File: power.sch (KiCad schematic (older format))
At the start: 26 parts, among them U24 TLV62569P, U26 TLV62569P, U27 TLV62569P

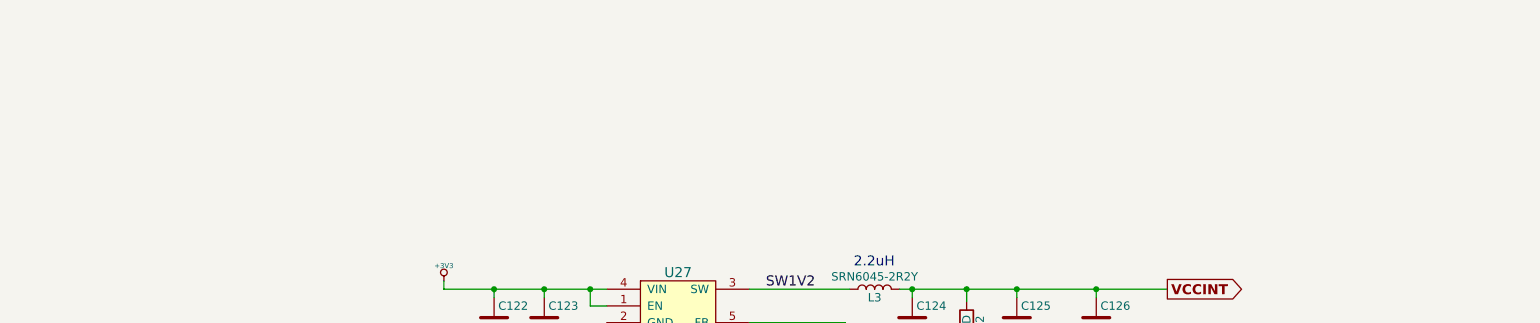
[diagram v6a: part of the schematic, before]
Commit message: VCCA and VCCD_PLL
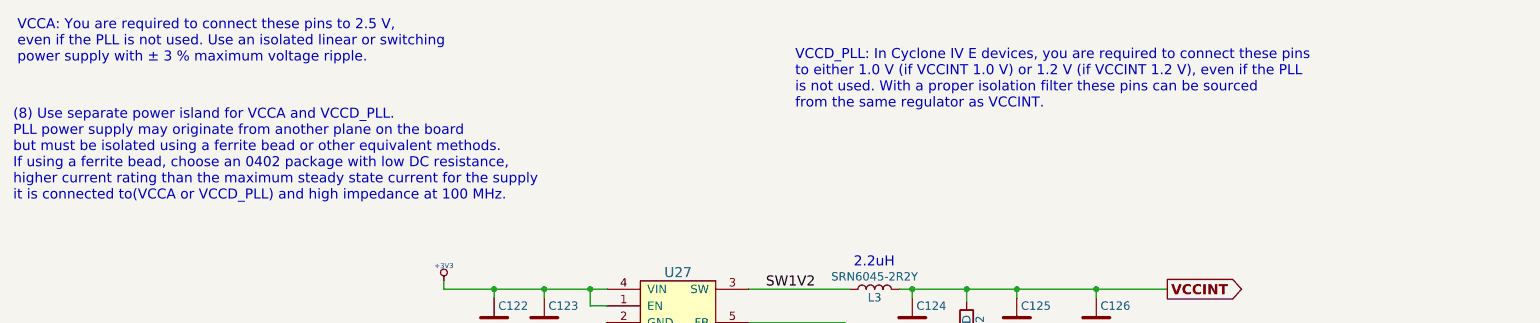
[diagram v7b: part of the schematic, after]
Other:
- note added: "(8) Use separate power island for VCCA and VCCD_PLL. \nPLL power supply may originate from another plane on the board \nbut must be isolated using a ferrite bead or other equivalent methods. \nIf using a ferrite bead, choose an 0402 package with low DC resistance, \nhigher current rating than the maximum steady state current for the supply \nit is connected to(VCCA or VCCD_PLL) and high impedance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"
- note added: "VCCA: You are required to connect these pins to 2.5 V, \neven if the PLL is not used. Use an isolated linear or switching \npower supply with ± 3 % maximum voltage ripple."
- note added: "VCCD_PLL: In Cyclone IV E devices, you are required to connect these pins \nto either 1.0 V (if VCCINT 1.0 V) or 1.2 V (if VCCINT 1.2 V), even if the PLL \nis not used. With a proper isolation filter these pins can be sourced \nfrom the same regulator as VCCINT."
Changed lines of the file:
@@
 $EndComp
 $Comp
-L GND #PWR0182
+L GND #PWR0186
 U 1 1 588CA667
 P 4500 3850
-F 0 "#PWR0182" H 4500 3600 50  0001 C CNN
+F 0 "#PWR0186" H 4500 3600 50  0001 C CNN
 F 1 "GND" H 4500 3700 50  0001 C CNN
 F 2 "" H 4500 3850 50  0000 C CNN
@@
 Connection ~ 4125 3650
 $Comp
-L GND #PWR0183
+L GND #PWR0187
 U 1 1 588CA72B
 P 4125 4000
-F 0 "#PWR0183" H 4125 3750 50  0001 C CNN
+F 0 "#PWR0187" H 4125 3750 50  0001 C CNN
 F 1 "GND" H 4125 3850 50  0001 C CNN
 F 2 "" H 4125 4000 50  0000 C CNN
@@
 	6650 4025 6650 4175
 $Comp
-L GND #PWR0184
+L GND #PWR0188
 U 1 1 588CB06D
 P 6650 4475
-F 0 "#PWR0184" H 6650 4225 50  0001 C CNN
+F 0 "#PWR0188" H 6650 4225 50  0001 C CNN
 F 1 "GND" H 6650 4325 50  0001 C CNN
 F 2 "" H 6650 4475 50  0000 C CNN
@@
 $EndComp
 $Comp
-L GND #PWR0185
+L GND #PWR0189
 U 1 1 588CB1AB
 P 6325 4000
-F 0 "#PWR0185" H 6325 3750 50  0001 C CNN
+F 0 "#PWR0189" H 6325 3750 50  0001 C CNN
 F 1 "GND" H 6325 3850 50  0001 C CNN
 F 2 "" H 6325 4000 50  0000 C CNN
@@
 +1V8
 $Comp
-L +5VDC #PWR0186
+L +5VDC #PWR0190
 U 1 1 588CF502
 P 3525 3600
-F 0 "#PWR0186" H 3625 3650 20  0001 C CNN
+F 0 "#PWR0190" H 3625 3650 20  0001 C CNN
 F 1 "+5VDC" H 3525 3690 30  0000 C CNN
 F 2 "" H 3525 3600 60  0000 C CNN
@@
 Connection ~ 3825 3650
 $Comp
-L GND #PWR0187
+L GND #PWR0191
 U 1 1 588D28B5
 P 3825 4000
-F 0 "#PWR0187" H 3825 3750 50  0001 C CNN
+F 0 "#PWR0191" H 3825 3750 50  0001 C CNN
 F 1 "GND" H 3825 3850 50  0001 C CNN
 F 2 "" H 3825 4000 50  0000 C CNN
@@
 $EndComp
 $Comp
-L GND #PWR0188
+L GND #PWR0192
 U 1 1 58A65167
 P 4500 5175
-F 0 "#PWR0188" H 4500 4925 50  0001 C CNN
+F 0 "#PWR0192" H 4500 4925 50  0001 C CNN
 F 1 "GND" H 4500 5025 50  0001 C CNN
 F 2 "" H 4500 5175 50  0000 C CNN
@@
 Connection ~ 4125 4975
 $Comp
-L GND #PWR0189
+L GND #PWR0193
 U 1 1 58A6517D
 P 4125 5325
-F 0 "#PWR0189" H 4125 5075 50  0001 C CNN
+F 0 "#PWR0193" H 4125 5075 50  0001 C CNN
 F 1 "GND" H 4125 5175 50  0001 C CNN
 F 2 "" H 4125 5325 50  0000 C CNN
@@
 	6650 5350 6650 5500
 $Comp
-L GND #PWR0190
+L GND #PWR0194
 U 1 1 58A6519F
 P 6650 5800
-F 0 "#PWR0190" H 6650 5550 50  0001 C CNN
+F 0 "#PWR0194" H 6650 5550 50  0001 C CNN
 F 1 "GND" H 6650 5650 50  0001 C CNN
 F 2 "" H 6650 5800 50  0000 C CNN
@@
 $EndComp
 $Comp
-L GND #PWR0191
+L GND #PWR0195
 U 1 1 58A651B1
 P 6325 5325
-F 0 "#PWR0191" H 6325 5075 50  0001 C CNN
+F 0 "#PWR0195" H 6325 5075 50  0001 C CNN
 F 1 "GND" H 6325 5175 50  0001 C CNN
 F 2 "" H 6325 5325 50  0000 C CNN
@@
 Connection ~ 3825 4975
 $Comp
-L GND #PWR0192
+L GND #PWR0196
 U 1 1 58A651D3
 P 3825 5325
-F 0 "#PWR0192" H 3825 5075 50  0001 C CNN
+F 0 "#PWR0196" H 3825 5075 50  0001 C CNN
 F 1 "GND" H 3825 5175 50  0001 C CNN
 F 2 "" H 3825 5325 50  0000 C CNN
@@
 $EndComp
 $Comp
-L GND #PWR0193
+L GND #PWR0197
 U 1 1 58A65EC4
 P 7425 5325
-F 0 "#PWR0193" H 7425 5075 50  0001 C CNN
+F 0 "#PWR0197" H 7425 5075 50  0001 C CNN
 F 1 "GND" H 7425 5175 50  0001 C CNN
 F 2 "" H 7425 5325 50  0000 C CNN
@@
 Connection ~ 7425 4975
 $Comp
-L +5VDC #PWR0194
+L +5VDC #PWR0198
 U 1 1 58A651C3
 P 3525 4925
-F 0 "#PWR0194" H 3625 4975 20  0001 C CNN
+F 0 "#PWR0198" H 3625 4975 20  0001 C CNN
 F 1 "+5VDC" H 3525 5015 30  0000 C CNN
 F 2 "" H 3525 4925 60  0000 C CNN
@@
 $EndComp
 $Comp
-L GND #PWR0195
+L GND #PWR0199
 U 1 1 58A865FA
 P 4500 2550
-F 0 "#PWR0195" H 4500 2300 50  0001 C CNN
+F 0 "#PWR0199" H 4500 2300 50  0001 C CNN
 F 1 "GND" H 4500 2400 50  0001 C CNN
 F 2 "" H 4500 2550 50  0000 C CNN
@@
 Connection ~ 4125 2350
 $Comp
-L GND #PWR0196
+L GND #PWR0200
 U 1 1 58A8660D
 P 4125 2700
-F 0 "#PWR0196" H 4125 2450 50  0001 C CNN
+F 0 "#PWR0200" H 4125 2450 50  0001 C CNN
 F 1 "GND" H 4125 2550 50  0001 C CNN
 F 2 "" H 4125 2700 50  0000 C CNN
@@
 	6650 2725 6650 2875
 $Comp
-L GND #PWR0197
+L GND #PWR0201
 U 1 1 58A8662B
 P 6650 3175
-F 0 "#PWR0197" H 6650 2925 50  0001 C CNN
+F 0 "#PWR0201" H 6650 2925 50  0001 C CNN
 F 1 "GND" H 6650 3025 50  0001 C CNN
 F 2 "" H 6650 3175 50  0000 C CNN
@@
 $EndComp
 $Comp
-L GND #PWR0198
+L GND #PWR0202
 U 1 1 58A8663C
 P 6325 2700
-F 0 "#PWR0198" H 6325 2450 50  0001 C CNN
+F 0 "#PWR0202" H 6325 2450 50  0001 C CNN
 F 1 "GND" H 6325 2550 50  0001 C CNN
 F 2 "" H 6325 2700 50  0000 C CNN
@@
 Connection ~ 3825 2350
 $Comp
-L GND #PWR0199
+L GND #PWR0203
 U 1 1 58A86658
 P 3825 2700
-F 0 "#PWR0199" H 3825 2450 50  0001 C CNN
+F 0 "#PWR0203" H 3825 2450 50  0001 C CNN
 F 1 "GND" H 3825 2550 50  0001 C CNN
 F 2 "" H 3825 2700 50  0000 C CNN
@@
 $EndComp
 $Comp
-L GND #PWR0200
+L GND #PWR0204
 U 1 1 58A86668
 P 7425 2700
-F 0 "#PWR0200" H 7425 2450 50  0001 C CNN
+F 0 "#PWR0204" H 7425 2450 50  0001 C CNN
 F 1 "GND" H 7425 2550 50  0001 C CNN
 F 2 "" H 7425 2700 50  0000 C CNN
@@
 Connection ~ 7425 2350
 $Comp
-L +3V3 #PWR0201
+L +3V3 #PWR0205
 U 1 1 58A86765
 P 3525 2300
-F 0 "#PWR0201" H 3625 2350 20  0001 C CNN
+F 0 "#PWR0205" H 3625 2350 20  0001 C CNN
 F 1 "+3V3" H 3525 2390 30  0000 C CNN
 F 2 "" H 3525 2300 60  0000 C CNN
@@
 	1    0    0    -1
 $EndComp
+Text Notes 975  1000 0    60   ~ 0
+VCCA: You are required to connect these pins to 2.5 V, \neven if the PLL is not used. Use an isolated linear or switching \npower supply with ± 3 % maximum voltage ripple.
+Text Notes 950  1825 0    60   ~ 0
+(8) Use separate power island for VCCA and VCCD_PLL. \nPLL power supply may originate from another plane on the board \nbut must be isolated using a ferrite bead or other equivalent methods. \nIf using a ferrite bead, choose an 0402 package with low DC resistance, \nhigher current rating than the maximum steady state current for the supply \nit is connected to(VCCA or VCCD_PLL) and high impedance at 100 MHz.
+Text Notes 5625 1275 0    60   ~ 0
+VCCD_PLL: In Cyclone IV E devices, you are required to connect these pins \nto either 1.0 V (if VCCINT 1.0 V) or 1.2 V (if VCCINT 1.2 V), even if the PLL \nis not used. With a proper isolation filter these pins can be sourced \nfrom the same regulator as VCCINT.
 $EndSCHEMATC

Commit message: VCCA added
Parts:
- added C129: 1,0, Capacitors_SMD:C_0805, symbol C
- added C130: 10n, Capacitors_SMD:C_0603, symbol C
- added C131: 2,2, Capacitors_SMD:C_0805, symbol C
- added C? (x2): 0,1, Capacitors_SMD:C_0402, symbol C
- added U28: LP2985-25, TO_SOT_Packages_SMD:SOT-23-5, symbol LP2985LV
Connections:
- net GND: now also C129.2, C130.2, C131.2, C?.2, C?.2, U28.2 (GND)
- new net: C129.1, U28.1 (VIN), U28.3 (ON/OFF)
- new net: C130.1, U28.4 (BYPASS)
- new net +2V5: C131.1, C?.1, C?.1, U28.5 (VOUT)
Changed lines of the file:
@@
 EESchema Schematic File Version 2
-LIBS:Sputnik-rescue
 LIBS:sputnik
 LIBS:power
@@
 LIBS:Winbond
 LIBS:Sputnik-cache
-EELAYER 26 0
+EELAYER 25 0
 EELAYER END
 $Descr A4 11693 8268
@@
 $EndComp
 $Comp
-L GND #PWR0186
+L GND #PWR0187
 U 1 1 588CA667
 P 4500 3850
-F 0 "#PWR0186" H 4500 3600 50  0001 C CNN
+F 0 "#PWR0187" H 4500 3600 50  0001 C CNN
 F 1 "GND" H 4500 3700 50  0001 C CNN
 F 2 "" H 4500 3850 50  0000 C CNN
@@
 Connection ~ 4125 3650
 $Comp
-L GND #PWR0187
+L GND #PWR0188
 U 1 1 588CA72B
 P 4125 4000
-F 0 "#PWR0187" H 4125 3750 50  0001 C CNN
+F 0 "#PWR0188" H 4125 3750 50  0001 C CNN
 F 1 "GND" H 4125 3850 50  0001 C CNN
 F 2 "" H 4125 4000 50  0000 C CNN
@@
 	6650 4025 6650 4175
 $Comp
-L GND #PWR0188
+L GND #PWR0189
 U 1 1 588CB06D
 P 6650 4475
-F 0 "#PWR0188" H 6650 4225 50  0001 C CNN
+F 0 "#PWR0189" H 6650 4225 50  0001 C CNN
 F 1 "GND" H 6650 4325 50  0001 C CNN
 F 2 "" H 6650 4475 50  0000 C CNN
@@
 $EndComp
 $Comp
-L GND #PWR0189
+L GND #PWR0190
 U 1 1 588CB1AB
 P 6325 4000
-F 0 "#PWR0189" H 6325 3750 50  0001 C CNN
+F 0 "#PWR0190" H 6325 3750 50  0001 C CNN
 F 1 "GND" H 6325 3850 50  0001 C CNN
 F 2 "" H 6325 4000 50  0000 C CNN
@@
 +1V8
 $Comp
-L +5VDC #PWR0190
+L +5VDC #PWR0191
 U 1 1 588CF502
 P 3525 3600
-F 0 "#PWR0190" H 3625 3650 20  0001 C CNN
+F 0 "#PWR0191" H 3625 3650 20  0001 C CNN
 F 1 "+5VDC" H 3525 3690 30  0000 C CNN
 F 2 "" H 3525 3600 60  0000 C CNN
@@
 Connection ~ 3825 3650
 $Comp
-L GND #PWR0191
+L GND #PWR0192
 U 1 1 588D28B5
 P 3825 4000
-F 0 "#PWR0191" H 3825 3750 50  0001 C CNN
+F 0 "#PWR0192" H 3825 3750 50  0001 C CNN
 F 1 "GND" H 3825 3850 50  0001 C CNN
 F 2 "" H 3825 4000 50  0000 C CNN
@@
 $EndComp
 $Comp
-L GND #PWR0192
+L GND #PWR0193
 U 1 1 58A65167
 P 4500 5175
-F 0 "#PWR0192" H 4500 4925 50  0001 C CNN
+F 0 "#PWR0193" H 4500 4925 50  0001 C CNN
 F 1 "GND" H 4500 5025 50  0001 C CNN
 F 2 "" H 4500 5175 50  0000 C CNN
@@
 Connection ~ 4125 4975
 $Comp
-L GND #PWR0193
+L GND #PWR0194
 U 1 1 58A6517D
 P 4125 5325
-F 0 "#PWR0193" H 4125 5075 50  0001 C CNN
+F 0 "#PWR0194" H 4125 5075 50  0001 C CNN
 F 1 "GND" H 4125 5175 50  0001 C CNN
 F 2 "" H 4125 5325 50  0000 C CNN
@@
 	6650 5350 6650 5500
 $Comp
-L GND #PWR0194
+L GND #PWR0195
 U 1 1 58A6519F
 P 6650 5800
-F 0 "#PWR0194" H 6650 5550 50  0001 C CNN
+F 0 "#PWR0195" H 6650 5550 50  0001 C CNN
 F 1 "GND" H 6650 5650 50  0001 C CNN
 F 2 "" H 6650 5800 50  0000 C CNN
@@
 $EndComp
 $Comp
-L GND #PWR0195
+L GND #PWR0196
 U 1 1 58A651B1
 P 6325 5325
-F 0 "#PWR0195" H 6325 5075 50  0001 C CNN
+F 0 "#PWR0196" H 6325 5075 50  0001 C CNN
 F 1 "GND" H 6325 5175 50  0001 C CNN
 F 2 "" H 6325 5325 50  0000 C CNN
@@
 Connection ~ 3825 4975
 $Comp
-L GND #PWR0196
+L GND #PWR0197
 U 1 1 58A651D3
 P 3825 5325
-F 0 "#PWR0196" H 3825 5075 50  0001 C CNN
+F 0 "#PWR0197" H 3825 5075 50  0001 C CNN
 F 1 "GND" H 3825 5175 50  0001 C CNN
 F 2 "" H 3825 5325 50  0000 C CNN
@@
 $EndComp
 $Comp
-L GND #PWR0197
+L GND #PWR0198
 U 1 1 58A65EC4
 P 7425 5325
-F 0 "#PWR0197" H 7425 5075 50  0001 C CNN
+F 0 "#PWR0198" H 7425 5075 50  0001 C CNN
 F 1 "GND" H 7425 5175 50  0001 C CNN
 F 2 "" H 7425 5325 50  0000 C CNN
@@
 Connection ~ 7425 4975
 $Comp
-L +5VDC #PWR0198
+L +5VDC #PWR0199
 U 1 1 58A651C3
 P 3525 4925
-F 0 "#PWR0198" H 3625 4975 20  0001 C CNN
+F 0 "#PWR0199" H 3625 4975 20  0001 C CNN
 F 1 "+5VDC" H 3525 5015 30  0000 C CNN
 F 2 "" H 3525 4925 60  0000 C CNN
@@
 $EndComp
 $Comp
-L GND #PWR0199
+L GND #PWR0200
 U 1 1 58A865FA
 P 4500 2550
-F 0 "#PWR0199" H 4500 2300 50  0001 C CNN
+F 0 "#PWR0200" H 4500 2300 50  0001 C CNN
 F 1 "GND" H 4500 2400 50  0001 C CNN
 F 2 "" H 4500 2550 50  0000 C CNN
@@
 Connection ~ 4125 2350
 $Comp
-L GND #PWR0200
+L GND #PWR0201
 U 1 1 58A8660D
 P 4125 2700
-F 0 "#PWR0200" H 4125 2450 50  0001 C CNN
+F 0 "#PWR0201" H 4125 2450 50  0001 C CNN
 F 1 "GND" H 4125 2550 50  0001 C CNN
 F 2 "" H 4125 2700 50  0000 C CNN
@@
 	6650 2725 6650 2875
 $Comp
-L GND #PWR0201
+L GND #PWR0202
 U 1 1 58A8662B
 P 6650 3175
-F 0 "#PWR0201" H 6650 2925 50  0001 C CNN
+F 0 "#PWR0202" H 6650 2925 50  0001 C CNN
 F 1 "GND" H 6650 3025 50  0001 C CNN
 F 2 "" H 6650 3175 50  0000 C CNN
@@
 $EndComp
 $Comp
-L GND #PWR0202
+L GND #PWR0203
 U 1 1 58A8663C
 P 6325 2700
-F 0 "#PWR0202" H 6325 2450 50  0001 C CNN
+F 0 "#PWR0203" H 6325 2450 50  0001 C CNN
 F 1 "GND" H 6325 2550 50  0001 C CNN
 F 2 "" H 6325 2700 50  0000 C CNN
@@
 Connection ~ 3825 2350
 $Comp
-L GND #PWR0203
+L GND #PWR0204
 U 1 1 58A86658
 P 3825 2700
-F 0 "#PWR0203" H 3825 2450 50  0001 C CNN
+F 0 "#PWR0204" H 3825 2450 50  0001 C CNN
 F 1 "GND" H 3825 2550 50  0001 C CNN
 F 2 "" H 3825 2700 50  0000 C CNN
@@
 $EndComp
 $Comp
-L GND #PWR0204
+L GND #PWR0205
 U 1 1 58A86668
 P 7425 2700
-F 0 "#PWR0204" H 7425 2450 50  0001 C CNN
+F 0 "#PWR0205" H 7425 2450 50  0001 C CNN
 F 1 "GND" H 7425 2550 50  0001 C CNN
 F 2 "" H 7425 2700 50  0000 C CNN
@@
 Connection ~ 7425 2350
 $Comp
-L +3V3 #PWR0205
+L +3V3 #PWR0206
 U 1 1 58A86765
 P 3525 2300
-F 0 "#PWR0205" H 3625 2350 20  0001 C CNN
+F 0 "#PWR0206" H 3625 2350 20  0001 C CNN
 F 1 "+3V3" H 3525 2390 30  0000 C CNN
 F 2 "" H 3525 2300 60  0000 C CNN
@@
 Text Notes 5625 1275 0    60   ~ 0
 VCCD_PLL: In Cyclone IV E devices, you are required to connect these pins \nto either 1.0 V (if VCCINT 1.0 V) or 1.2 V (if VCCINT 1.2 V), even if the PLL \nis not used. With a proper isolation filter these pins can be sourced \nfrom the same regulator as VCCINT.
+$Comp
+L LP2985LV U28
+U 1 1 58B4A36C
+P 4950 6550
+F 0 "U28" H 5150 6100 50  0000 C CNN
+F 1 "LP2985-25" H 4950 7000 50  0000 C CNN
+F 2 "TO_SOT_Packages_SMD:SOT-23-5" H 4950 6550 50  0000 C CNN
+F 3 "" H 4950 6550 50  0000 C CNN
+	1    4950 6550
+	1    0    0    -1
+$EndComp
+$Comp
+L GND #PWR0207
+U 1 1 58B4A4E6
+P 4950 7250
+F 0 "#PWR0207" H 4950 7000 50  0001 C CNN
+F 1 "GND" H 4950 7100 50  0001 C CNN
+F 2 "" H 4950 7250 50  0000 C CNN
+F 3 "" H 4950 7250 50  0000 C CNN
+F 4 "Value" H 4950 7250 60  0001 C CNN "Fieldname"
+	1    4950 7250
+	1    0    0    -1
+$EndComp
+$Comp
+L C C129
+U 1 1 58B4A5F4
+P 3800 6475
+F 0 "C129" H 3825 6575 50  0000 L CNN
+F 1 "1,0" H 3825 6375 50  0000 L CNN
+F 2 "Capacitors_SMD:C_0805" H 3838 6325 50  0001 C CNN
+F 3 "" H 3800 6475 50  0000 C CNN
+	1    3800 6475
+	1    0    0    -1
+$EndComp
+Wire Wire Line
+	3575 6250 4150 6250
+Wire Wire Line
+	3800 6250 3800 6325
+Connection ~ 3800 6250
+Wire Wire Line
+	4050 6450 4150 6450
+Wire Wire Line
+	4050 6250 4050 6450
+Connection ~ 4050 6250
+$Comp
+L GND #PWR0208
+U 1 1 58B4A801
+P 3800 6625
+F 0 "#PWR0208" H 3800 6375 50  0001 C CNN
+F 1 "GND" H 3800 6475 50  0001 C CNN
+F 2 "" H 3800 6625 50  0000 C CNN
+F 3 "" H 3800 6625 50  0000 C CNN
+F 4 "Value" H 3800 6625 60  0001 C CNN "Fieldname"
+	1    3800 6625
+	1    0    0    -1
+$EndComp
+$Comp
+L C C130
+U 1 1 58B4A8DB
+P 4050 7000
+F 0 "C130" H 4075 7100 50  0000 L CNN
+F 1 "10n" H 4075 6900 50  0000 L CNN
+F 2 "Capacitors_SMD:C_0603" H 4088 6850 50  0001 C CNN
+F 3 "" H 4050 7000 50  0000 C CNN
+	1    4050 7000
+	1    0    0    -1
+$EndComp
+Wire Wire Line
+	4150 6750 4050 6750
+Wire Wire Line
+	4050 6750 4050 6850
+$Comp
+L GND #PWR0209
+U 1 1 58B4AA37
+P 4050 7150
+F 0 "#PWR0209" H 4050 6900 50  0001 C CNN
+F 1 "GND" H 4050 7000 50  0001 C CNN
+F 2 "" H 4050 7150 50  0000 C CNN
+F 3 "" H 4050 7150 50  0000 C CNN
+F 4 "Value" H 4050 7150 60  0001 C CNN "Fieldname"
+	1    4050 7150
+	1    0    0    -1
+$EndComp
+Wire Wire Line
+	5750 6250 6800 6250
+Text GLabel 6800 6250 2    60   Output ~ 12
++2V5
+$Comp
+L C C131
+U 1 1 58B4BFE9
+P 5925 6500
+F 0 "C131" H 5950 6600 50  0000 L CNN
+F 1 "2,2" H 5950 6400 50  0000 L CNN
+F 2 "Capacitors_SMD:C_0805" H 5963 6350 50  0001 C CNN
+F 3 "" H 5925 6500 50  0000 C CNN
+	1    5925 6500
+	1    0    0    -1
+$EndComp
+Wire Wire Line
+	5925 6350 5925 6250
+Connection ~ 5925 6250
+$Comp
+L GND #PWR0210
+U 1 1 58B4C102
+P 5925 6650
+F 0 "#PWR0210" H 5925 6400 50  0001 C CNN
+F 1 "GND" H 5925 6500 50  0001 C CNN
+F 2 "" H 5925 6650 50  0000 C CNN
+F 3 "" H 5925 6650 50  0000 C CNN
+F 4 "Value" H 5925 6650 60  0001 C CNN "Fieldname"
+	1    5925 6650
+	1    0    0    -1
+$EndComp
+$Comp
+L C C?
+U 1 1 58B4F242
+P 6400 6500
+F 0 "C?" H 6425 6600 50  0000 L CNN
+F 1 "0,1" H 6425 6400 50  0000 L CNN
+F 2 "Capacitors_SMD:C_0402" H 6438 6350 50  0001 C CNN
+F 3 "" H 6400 6500 50  0000 C CNN
+	1    6400 6500
+	1    0    0    -1
+$EndComp
+$Comp
+L C C?
+U 1 1 58B4F355
+P 6650 6500
+F 0 "C?" H 6675 6600 50  0000 L CNN
+F 1 "0,1" H 6675 6400 50  0000 L CNN
+F 2 "Capacitors_SMD:C_0402" H 6688 6350 50  0001 C CNN
+F 3 "" H 6650 6500 50  0000 C CNN
+	1    6650 6500
+	1    0    0    -1
+$EndComp
+Wire Wire Line
+	6650 6350 6650 6250
+Connection ~ 6650 6250
+Wire Wire Line
+	6400 6350 6400 6250
+Connection ~ 6400 6250
+$Comp
+L GND #PWR?
+U 1 1 58B4F4E9
+P 6400 6650
+F 0 "#PWR?" H 6400 6400 50  0001 C CNN
+F 1 "GND" H 6400 6500 50  0001 C CNN
+F 2 "" H 6400 6650 50  0000 C CNN
+F 3 "" H 6400 6650 50  0000 C CNN
+F 4 "Value" H 6400 6650 60  0001 C CNN "Fieldname"
+	1    6400 6650
+	1    0    0    -1
+$EndComp
+$Comp
+L GND #PWR?
+U 1 1 58B4F556
+P 6650 6650
+F 0 "#PWR?" H 6650 6400 50  0001 C CNN
+F 1 "GND" H 6650 6500 50  0001 C CNN
+F 2 "" H 6650 6650 50  0000 C CNN
+F 3 "" H 6650 6650 50  0000 C CNN
+F 4 "Value" H 6650 6650 60  0001 C CNN "Fieldname"
+	1    6650 6650
+	1    0    0    -1
+$EndComp
 $EndSCHEMATC
